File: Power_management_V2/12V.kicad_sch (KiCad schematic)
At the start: 29 parts, among them U5 SIC43x

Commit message: Hoan thanh SCH mach Power
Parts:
- removed C21: 22u, Library:C_CER_7.5x6.3, symbol Device:C
- removed C25: 100n, Library:C_0603_1608Metric, symbol Device:C
- removed C27: 4.7u, Library:C_1206_3216Metric, symbol Device:C
- removed C28: 1u, Library:C_0603_1608Metric, symbol Device:C
- removed C34, C35, C36, C37, C38, C39, C40, C41: 22u, Library:C_1210_3225Metric, symbol Device:C
- removed L5: 2.2u, Library:L_Vishay_IHLP-6767, symbol Device:L
- removed R19: 2.2, Library:R_0603_1608Metric, symbol Device:R
- removed R20, R21, R22: 100k, Library:R_0603_1608Metric, symbol Device:R
- removed R23: 10k, Library:R_0603_1608Metric, symbol Device:R
- removed U5: SIC43x, Library:SIC43x, symbol RM_Converter_DCDC:SIC43x
- added C11, C12, C18, C19, C20: 22u/50V/3025, Library:C_CER_7.5x6.3, symbol Device:C
- added C13, C14, C17: 100n/50V/0603, Library:C_0603_1608Metric, symbol Device:C
- added C15: 4.7u/16V/1206, Library:C_1206_3216Metric, symbol Device:C
- added C16: 1u/16V/0603, Library:C_0603_1608Metric, symbol Device:C
- added L1: 2.2u/22A, symbol Device:L
- added R3, R5, R6, R7: 100k/0603, Library:R_0603_1608Metric, symbol Device:R
- added R4: 2.2R/0603, Library:R_0603_1608Metric, symbol Device:R
- added R8: 10k/0603/0.1%, Library:R_0603_1608Metric, symbol Device:R
- added U1: SIC43x, Library:SIC43x, symbol RM_Converter_DCDC:SIC43x
- C22, C23, C24: value 22u -> 22u/50V/3025
- C26: value 100n -> 22u/50V/3025; footprint Library:C_0603_1608Metric -> Library:C_CER_7.5x6.3; Coefficient X7R -> X79; Digikey 587-1243-1-ND -> 445-174338-1-ND; Manufacturer Taiyo Yuden -> United Chemi-Con; Part UMK107B7104KA-T -> KTS500B226M76N0T00; Tolerance 10% -> 20
- C29: value 100n -> 100n/50V/0603
- C30, C31, C32, C33: value 22u -> 22u/50V/3025; footprint Library:C_1210_3225Metric -> Library:C_CER_7.5x6.3; Coefficient X7R -> X79; Digikey 1276-3392-1-ND -> 445-174338-1-ND; Manufacturer Samsung -> United Chemi-Con; Part CL32B226KAJNNNE -> KTS500B226M76N0T00; Tolerance 10% -> 20; Voltage 25 -> 50
- R14: renamed from R24; value 191K -> 191K/0603/0.1%; footprint Library:R_0603_1608Metric -> DipTek PSU library:R_0603_1608Metric; symbol Device:R -> DipTek PSU library:R
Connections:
- net GND: now also C26.2, C29.1, C11.2, C12.2, C13.1, C17.1, C18.2, C19.2, C20.2, U1.13 (PGND), U1.27 (PGND), U1.3 (PGND), U1.4 (PGND); no longer C29.2
- net GND1: now also C15.2, C16.2, R5.2, R8.1, U1.16 (AGND), U1.25 (AGND)
- net VBAT: now also C29.2, C11.1, C12.1, C13.2, R3.1, U1.1 (VIN), U1.2 (VIN), U1.22 (VIN), U1.26 (VIN); no longer C22.1, C23.1, C24.1
- net at R14.1: now also R8.2, U1.17 (FB)
- net VOUT_12V: now reaches C26.1
- net VOUT_12V: now also C22.1, C23.1, C24.1, C30.1, C31.1, C32.1, C33.1, R14.2, C17.2, C18.1, C19.1, C20.1, L1.2, U1.18 (VOUT)
- removed net VOUT: C29.1, C30.1, C31.1, C32.1, C33.1, R14.2
- new net: C16.1, R6.2, R7.1, U1.15 (VDD)
- new net: R5.1, U1.20 (MODE2)
- new net: R6.1, U1.14 (PGOOD)
- new net: R3.2, U1.19 (EN)
- new net: C14.1, U1.23 (BOOT)
- new net: C14.2, R4.2
- new net: R7.2, U1.21 (MODE1)
- new net: L1.1, U1.5 (SW), U1.6 (SW), U1.7 (SW), U1.8 (SW), U1.9 (SW)
- new net: R4.1, U1.24 (PHASE)
- new net: U1.10 (GL), U1.11 (GL), U1.28 (GL)
- new net: C15.1, U1.12 (VDRV)
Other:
- note added: "AGND and PGND connected inside SIC431"
- note added: "MODE selection MODE1 100K to VDD for forced CCM Fsw = 500kHz MODE2 OC limit of 17.3A 100K to AGND = 54% of Imax (32A - SIC431x)"
- note added: "Output Voltage ------- R_FB_H = R_FB_L(Vout-Vfb)/Vfb R_FB_H - Resistor Feedback High R_FB_L - Resistor feedback Low VOut - Desired output voltage Vfb - feedback voltage (0.6) ------ R_FB_H = 10000(12-0.6)/0.6 R_FB_H = 191k"
- note added: "SIC431AED-T1-GE3"
- note removed: "Output Voltage ------- R_FB_H = R_FB_L(Vout-Vfb)/Vfb R_FB_H - Resistor Feedback High R_FB_L - Resistor feedback Low VOut - Desired output voltage Vfb - feedback voltage (0.6) ------ R_FB_H = 10000(12-0.6)/0.6 R_FB_H = 190k"
- moved on the sheet: R14

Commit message: Hoan thanh SCH lan 1
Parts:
- renumbered C11 to C1, C19 to C10, C30 to C11, C20 to C12, C31 to C13, C22 to C14, C32 to C15, C23 to C16, C33 to C17, C24 to C18, C26 to C19, C12 to C2, C13 to C3, C29 to C4, C14 to C5, C15 to C6, C16 to C7, C17 to C8, C18 to C9, R3 to R1, R4 to R2, R5 to R3, R6 to R4, R7 to R5, R8 to R6, R14 to R7

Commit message: Chỉnh sủa SCH 24/12
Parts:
- removed R1: 100k/0603, Library:R_0603_1608Metric, symbol Device:R
- R3: value 100k/0603 -> 499k/0603; Digikey 311-100KHRCT-ND -> (none); Manufacturer YAGEO -> (none); Part RC0603FR-07100KL -> (none); Power 1/16 -> (none); Tolerance 1% -> (none)
- U1: Part SIC431AED-T1-GE3 -> SIC437AED-T1-GE3
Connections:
- net EN_12V: now reaches U1.19 (EN)
- now unconnected: U1.10 (GL), U1.11 (GL), U1.28 (GL)
- no-connect marks 0 -> 3
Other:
- note added: "AGND and PGND connected inside SIC437"
- note added: "MODE selection MODE1 100K to VDD for forced CCM Fsw = 500kHz MODE2 OC limit of 18A 499K to AGND = 100% of Imax (18A - SIC437x)"
- note added: "SIC437AED-T1-GE3"
- note removed: "AGND and PGND connected inside SIC431"
- note removed: "MODE selection MODE1 100K to VDD for forced CCM Fsw = 500kHz MODE2 OC limit of 17.3A 100K to AGND = 54% of Imax (32A - SIC431x)"
- note removed: "SIC431AED-T1-GE3"
- company: Raw Matter IO Pty Ltd -> (none)
- title: (none) -> Diptek Power Board V2
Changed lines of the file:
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@@
 	(paper "A4")
 	(title_block
+		(title "Diptek Power Board V2")
 		(date "2025-08-26")
-		(rev "1")
-		(company "Raw Matter IO Pty Ltd")
-		(comment 1 "Preliminary Design")
-		(comment 2 "Released for discussion")
-		(comment 3 "C28 updated")
+		(rev "2")
 	)
-	(text "SIC431AED-T1-GE3"
+	(text "SIC437AED-T1-GE3"
 		(exclude_from_sim no)
 		(at 128.27 117.475 0)
@@
 		)
 	)
-	(text "MODE selection\nMODE1\n100K to VDD for forced CCM\nFsw = 500kHz\n\nMODE2\nOC limit of 17.3A\n100K to AGND = 54% of Imax (32A - SIC431x)"
+	(text "MODE selection\nMODE1\n100K to VDD for forced CCM\nFsw = 500kHz\n\nMODE2\nOC limit of 18A\n499K to AGND = 100% of Imax (18A - SIC437x)"
 		(exclude_from_sim no)
 		(at 200.025 61.214 0)
@@
 		)
 	)
-	(text "AGND and PGND connected inside SIC431"
+	(text "AGND and PGND connected inside SIC437\n"
 		(exclude_from_sim no)
 		(at 220.599 73.66 0)
@@
 	)
 	(junction
-		(at 116.205 100.33)
-		(diameter 0)
-		(color 0 0 0 0)
-	)
-	(junction
 		(at 60.325 78.74)
 		(diameter 0)
@@
 	)
 	(junction
-		(at 85.09 71.12)
-		(diameter 0)
-		(color 0 0 0 0)
-	)
-	(junction
 		(at 70.485 78.74)
 		(diameter 0)
@@
 		(color 0 0 0 0)
 	)
-	(wire
-		(pts
-			(xy 228.6 116.84) (xy 238.125 116.84)
-		)
-		(stroke
-			(width 0)
-			(type default)
-		)
+	(no_connect
+		(at 116.078 100.33)
+	)
+	(no_connect
+		(at 116.078 102.87)
+	)
+	(no_connect
+		(at 116.078 97.79)
 	)
 	(wire
 		(pts
-			(xy 116.205 97.79) (xy 116.205 100.33)
+			(xy 228.6 116.84) (xy 238.125 116.84)
 		)
 		(stroke
@@
 	(wire
 		(pts
-			(xy 118.745 97.79) (xy 116.205 97.79)
+			(xy 116.078 97.79) (xy 118.745 97.79)
 		)
 		(stroke
@@
 	(wire
 		(pts
-			(xy 116.205 100.33) (xy 118.745 100.33)
+			(xy 116.078 100.33) (xy 118.745 100.33)
 		)
 		(stroke
@@
 	(wire
 		(pts
-			(xy 116.205 100.33) (xy 116.205 102.87)
-		)
-		(stroke
-			(width 0)
-			(type default)
-		)
-	)
-	(wire
-		(pts
 			(xy 140.335 111.76) (xy 169.545 111.76)
 		)
@@
 	(wire
 		(pts
-			(xy 90.17 78.74) (xy 85.09 78.74)
-		)
-		(stroke
-			(width 0)
-			(type default)
-		)
-	)
-	(wire
-		(pts
 			(xy 116.205 106.68) (xy 118.745 106.68)
 		)
@@
 	(wire
 		(pts
-			(xy 85.09 71.12) (xy 118.745 71.12)
-		)
-		(stroke
-			(width 0)
-			(type default)
-		)
-	)
-	(wire
-		(pts
-			(xy 78.74 71.12) (xy 85.09 71.12)
+			(xy 78.74 71.12) (xy 118.745 71.12)
 		)
 		(stroke
@@
 	(wire
 		(pts
-			(xy 85.09 78.74) (xy 85.09 71.12)
-		)
-		(stroke
-			(width 0)
-			(type default)
-		)
-	)
-	(wire
-		(pts
 			(xy 140.335 72.39) (xy 145.415 72.39)
 		)
@@
 	(wire
 		(pts
-			(xy 116.205 102.87) (xy 118.745 102.87)
+			(xy 116.078 102.87) (xy 118.745 102.87)
 		)
 		(stroke
@@
 		)
 	)
+	(hierarchical_label "EN_12V"
+		(shape input)
+		(at 97.79 78.74 180)
+		(effects
+			(font
+				(size 1.27 1.27)
+			)
+			(justify right)
+		)
+	)
 	(hierarchical_label "VBAT"
 		(shape input)
@@
 			)
 		)
-		(property "Value" "100k/0603"
+		(property "Value" "499k/0603"
 			(at 148.463 92.6521 0)
 			(effects
@@
 			)
 		)
-		(property "Digikey" "311-100KHRCT-ND"
+		(property "Digikey" ""
 			(at 146.685 91.44 0)
 			(effects
@@
 			)
 		)
-		(property "Power" "1/16"
+		(property "Power" ""
 			(at 146.685 91.44 0)
 			(effects
@@
 			)
 		)
-		(property "Tolerance" "1%"
+		(property "Tolerance" ""
 			(at 146.685 91.44 0)
 			(effects
@@
 			)
 		)
-		(property "Manufacturer" "YAGEO"
+		(property "Manufacturer" ""
 			(at 146.685 91.44 0)
 			(effects
@@
 			)
 		)
-		(property "Part" "RC0603FR-07100KL"
+		(property "Part" ""
 			(at 146.685 91.44 0)
 			(effects
@@
 	)
 	(symbol
-		(lib_id "Device:R")
-		(at 93.98 78.74 90)
-		(unit 1)
-		(exclude_from_sim no)
-		(in_bom yes)
-		(on_board yes)
-		(dnp no)
-		(fields_autoplaced yes)
-		(property "Reference" "R1"
-			(at 93.98 73.025 90)
-			(effects
-				(font
-					(size 1.27 1.27)
-				)
-			)
-		)
-		(property "Value" "100k/0603"
-			(at 93.98 75.565 90)
-			(effects
-				(font
-					(size 1.27 1.27)
-				)
-			)
-		)
-		(property "Footprint" "Library:R_0603_1608Metric"
-			(at 93.98 80.518 90)
-			(effects
-				(font
-					(size 1.27 1.27)
-				)
-				(hide yes)
-			)
-		)
-		(property "Datasheet" ""
-			(at 93.98 78.74 0)
-			(effects
-				(font
-					(size 1.27 1.27)
-				)
-				(hide yes)
-			)
-		)
-		(property "Description" "Resistor"
-			(at 93.98 78.74 0)
-			(effects
-				(font
-					(size 1.27 1.27)
-				)
-				(hide yes)
-			)
-		)
-		(property "Digikey" "311-100KHRCT-ND"
-			(at 93.98 78.74 0)
-			(effects
-				(font
-					(size 1.27 1.27)
-				)
-				(hide yes)
-			)
-		)
-		(property "Power" "1/16"
-			(at 93.98 78.74 0)
-			(effects
-				(font
-					(size 1.27 1.27)
-				)
-				(hide yes)
-			)
-		)
-		(property "Tolerance" "1%"
-			(at 93.98 78.74 0)
-			(effects
-				(font
-					(size 1.27 1.27)
-				)
-				(hide yes)
-			)
-		)
-		(property "Manufacturer" "YAGEO"
-			(at 93.98 78.74 0)
-			(effects
-				(font
-					(size 1.27 1.27)
-				)
-				(hide yes)
-			)
-		)
-		(property "Part" "RC0603FR-07100KL"
-			(at 93.98 78.74 0)
-			(effects
-				(font
-					(size 1.27 1.27)
-				)
-				(hide yes)
-			)
-		)
-		(pin "1"
-		)
-		(pin "2"
-		)
-		(instances
-			(project "Power_management_V2"
-				(path "/632966f8-0e72-49d8-ae31-468f807051b0/ea320acb-942d-4621-955d-3f03cfc2bafa"
-					(reference "R1")
-					(unit 1)
-				)
-			)
-		)
-	)
-	(symbol
 		(lib_id "Device:C")
 		(at 109.855 92.71 270)
@@
 			)
 		)
-		(property "Part" "SIC431AED-T1-GE3"
+		(property "Part" "SIC437AED-T1-GE3"
 			(at 130.175 86.36 0)
 			(effects

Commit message: Hoan thanh footprint
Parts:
- C3, C4, C5, C7, C8: footprint Library:C_0603_1608Metric -> Capacitor_SMD:C_0603_1608Metric
- L1: footprint (none) -> Library:IND_SRP1265A-2R2M
- R2, R3, R4, R5, R6: footprint Library:R_0603_1608Metric -> Resistor_SMD:R_0603_1608Metric
- R7: footprint DipTek PSU library:R_0603_1608Metric -> Resistor_SMD:R_0603_1608Metric
- U1: footprint Library:SIC43x -> Library:VREG_SIC437AED-T1-GE3

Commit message: hoan thanh sap xep
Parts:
- C10, C11, C12, C13, C14, C15, C16, C17, C18, C19, C9: value 22u/50V/3025 -> 22u/25V/1210; footprint Library:C_CER_7.5x6.3 -> Capacitor_SMD:C_1210_3225Metric
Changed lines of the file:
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@@
 			)
 		)
-		(property "Value" "22u/50V/3025"
+		(property "Value" "22u/25V/1210"
 			(at 198.755 152.4 90)
 			(effects
@@
 			)
 		)
-		(property "Footprint" "Library:C_CER_7.5x6.3"
+		(property "Footprint" "Capacitor_SMD:C_1210_3225Metric"
 			(at 204.1652 141.605 0)
 			(effects
@@
 			)
 		)
-		(property "Value" "22u/50V/3025"
+		(property "Value" "22u/25V/1210"
 			(at 214.63 127.635 90)
 			(effects
@@
 			)
 		)
-		(property "Footprint" "Library:C_CER_7.5x6.3"
+		(property "Footprint" "Capacitor_SMD:C_1210_3225Metric"
 			(at 220.0402 116.84 0)
 			(effects
@@
 			)
 		)
-		(property "Value" "22u/50V/3025"
+		(property "Value" "22u/25V/1210"
 			(at 205.105 127.635 90)
 			(effects
@@
 			)
 		)
-		(property "Footprint" "Library:C_CER_7.5x6.3"
+		(property "Footprint" "Capacitor_SMD:C_1210_3225Metric"
 			(at 210.5152 116.84 0)
 			(effects
@@
 			)
 		)
-		(property "Value" "22u/50V/3025"
+		(property "Value" "22u/25V/1210"
 			(at 224.155 127.635 90)
 			(effects
@@
 			)
 		)
-		(property "Footprint" "Library:C_CER_7.5x6.3"
+		(property "Footprint" "Capacitor_SMD:C_1210_3225Metric"
 			(at 229.5652 116.84 0)
 			(effects
@@
 			)
 		)
-		(property "Value" "22u/50V/3025"
+		(property "Value" "22u/25V/1210"
 			(at 195.58 127.635 90)
 			(effects
@@
 			)
 		)
-		(property "Footprint" "Library:C_CER_7.5x6.3"
+		(property "Footprint" "Capacitor_SMD:C_1210_3225Metric"
 			(at 200.9902 116.84 0)
 			(effects
@@
 			)
 		)
-		(property "Value" "22u/50V/3025"
+		(property "Value" "22u/25V/1210"
 			(at 233.68 127.635 90)
 			(effects
@@
 			)
 		)
-		(property "Footprint" "Library:C_CER_7.5x6.3"
+		(property "Footprint" "Capacitor_SMD:C_1210_3225Metric"
 			(at 239.0902 116.84 0)
 			(effects
@@
 			)
 		)
-		(property "Value" "22u/50V/3025"
+		(property "Value" "22u/25V/1210"
 			(at 208.28 152.4 90)
 			(effects
@@
 			)
 		)
-		(property "Footprint" "Library:C_CER_7.5x6.3"
+		(property "Footprint" "Capacitor_SMD:C_1210_3225Metric"
 			(at 213.6902 141.605 0)
 			(effects
@@
 			)
 		)
-		(property "Value" "22u/50V/3025"
+		(property "Value" "22u/25V/1210"
 			(at 243.205 127.635 90)
 			(effects
@@
 			)
 		)
-		(property "Footprint" "Library:C_CER_7.5x6.3"
+		(property "Footprint" "Capacitor_SMD:C_1210_3225Metric"
 			(at 248.6152 116.84 0)
 			(effects
@@
 			)
 		)
-		(property "Value" "22u/50V/3025"
+		(property "Value" "22u/25V/1210"
 			(at 186.055 124.46 90)
 			(effects
@@
 			)
 		)
-		(property "Footprint" "Library:C_CER_7.5x6.3"
+		(property "Footprint" "Capacitor_SMD:C_1210_3225Metric"
 			(at 190.8302 116.84 0)
 			(effects
@@
 			)
 		)
-		(property "Value" "22u/50V/3025"
+		(property "Value" "22u/25V/1210"
 			(at 227.33 152.4 90)
 			(effects
@@
 			)
 		)
-		(property "Footprint" "Library:C_CER_7.5x6.3"
+		(property "Footprint" "Capacitor_SMD:C_1210_3225Metric"
 			(at 232.7402 141.605 0)
 			(effects
@@
 			)
 		)
-		(property "Value" "22u/50V/3025"
+		(property "Value" "22u/25V/1210"
 			(at 217.805 152.4 90)
 			(effects
@@
 			)
 		)
-		(property "Footprint" "Library:C_CER_7.5x6.3"
+		(property "Footprint" "Capacitor_SMD:C_1210_3225Metric"
 			(at 223.2152 141.605 0)
 			(effects

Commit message: Hoan thien Sap xep Linh kien
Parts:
- removed C10, C11, C13, C15, C17: 22u/25V/1210, Capacitor_SMD:C_1210_3225Metric, symbol Device:C

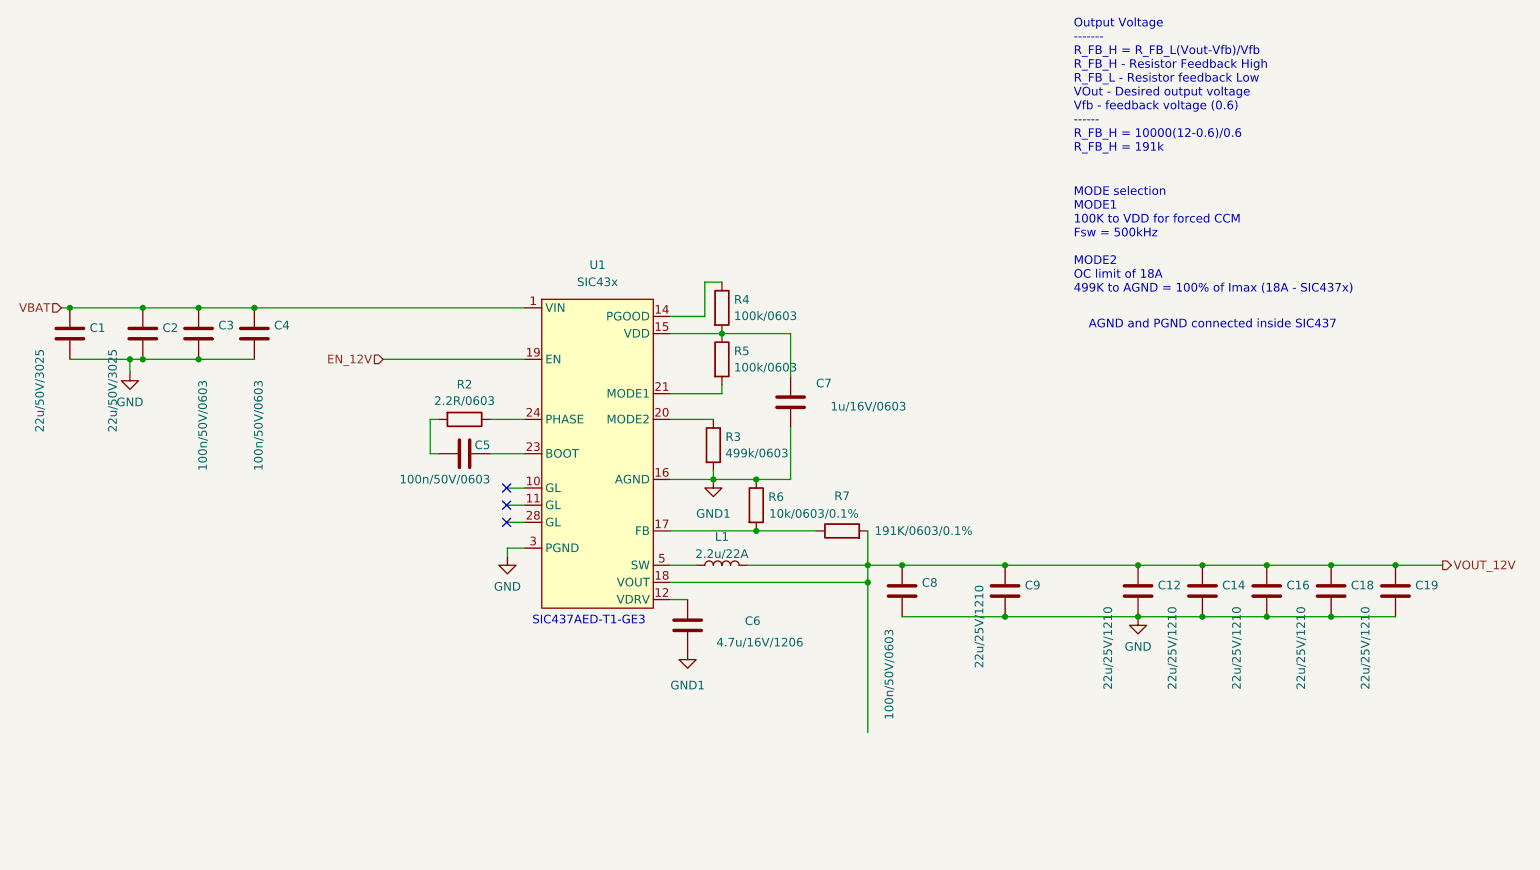
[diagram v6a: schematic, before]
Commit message: Cập nhật connecter 12 5
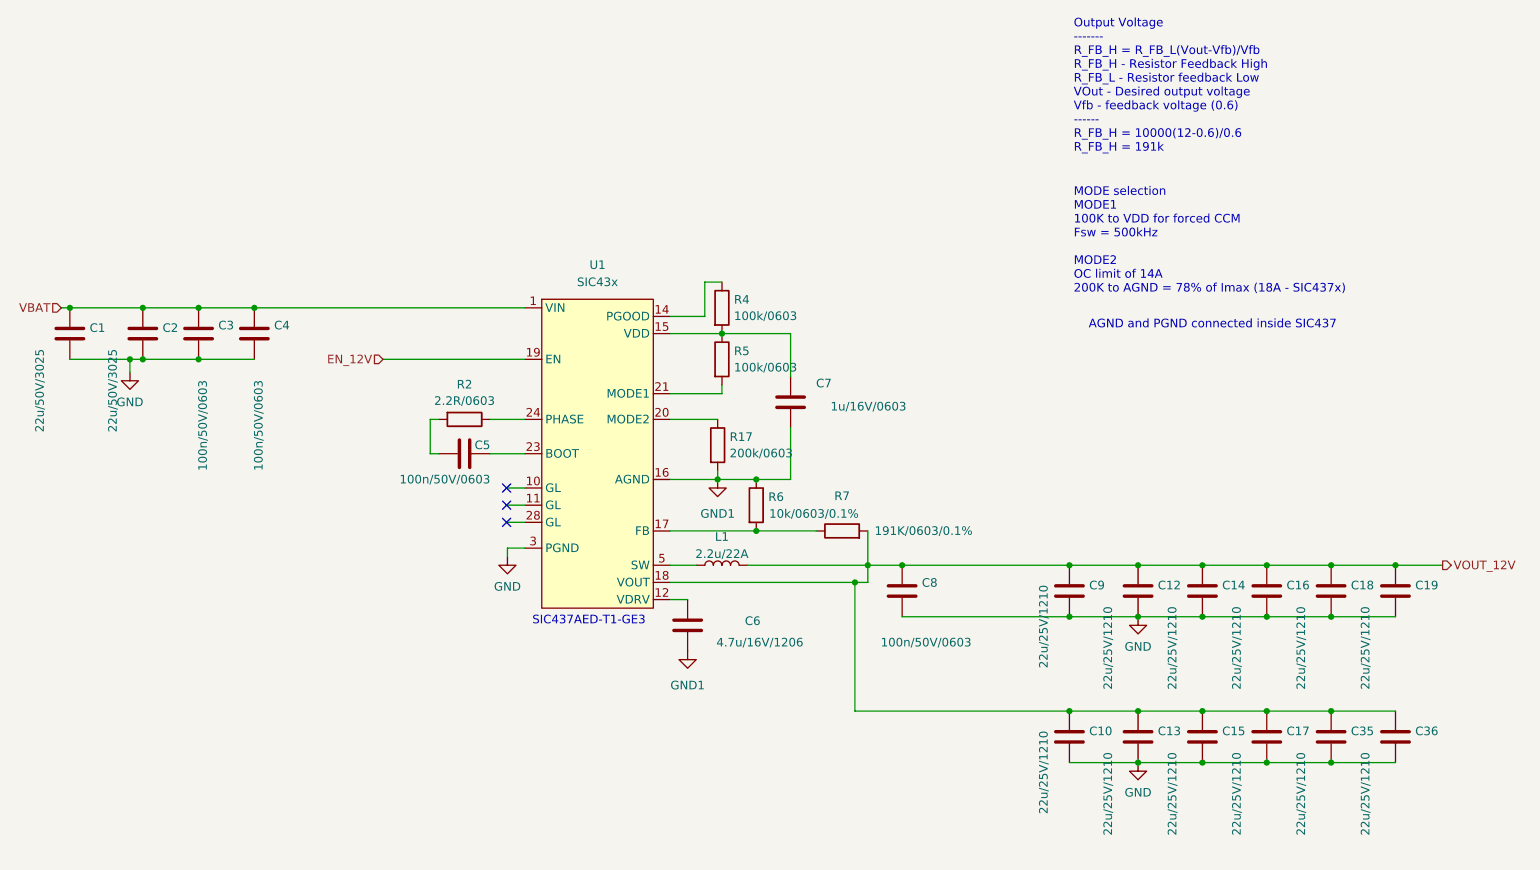
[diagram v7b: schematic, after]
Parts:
- removed R3: 499k/0603, Resistor_SMD:R_0603_1608Metric, symbol Device:R
- added C10, C13, C15, C17, C35, C36: 22u/25V/1210, Capacitor_SMD:C_1210_3225Metric, symbol Device:C
- added R17: 200k/0603, Resistor_SMD:R_0603_1608Metric, symbol Device:R
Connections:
- net GND: now also C10.2, C13.2, C15.2, C17.2, C35.2, C36.2
- net GND1: now also R17.2
- net VOUT_12V: now also C10.1, C13.1, C15.1, C17.1, C35.1, C36.1
- net at U1.20 (MODE2): now also R17.1
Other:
- note added: "MODE selection MODE1 100K to VDD for forced CCM Fsw = 500kHz MODE2 OC limit of 14A 200K to AGND = 78% of Imax (18A - SIC437x)"
- note removed: "MODE selection MODE1 100K to VDD for forced CCM Fsw = 500kHz MODE2 OC limit of 18A 499K to AGND = 100% of Imax (18A - SIC437x)"
- moved on the sheet: C9

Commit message: Layout 2201
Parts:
- removed C3: 100n/50V/0603, Capacitor_SMD:C_0603_1608Metric, symbol Device:C
- added NT2: NetTie_2, Library:NetTie-2_SMD_Pad1.56mm, symbol Device:NetTie_2
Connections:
- net GND: now also C6.2, NT2.2
- net GND1 renamed GND2
- net GND2: now also NT2.1; no longer C6.2
